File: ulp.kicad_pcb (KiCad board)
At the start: 2 copper layers, 102 x 84.2 mm, 49 parts, among them J1 Conn_01x01_Pin, J2 Conn_01x01_Pin, SW1 SW_Push_45deg, SW10 SW_Push_45deg, SW11 SW_Push_45deg, SW12 SW_Push_45deg, SW13 SW_Push_45deg, SW14 SW_Push_45deg, SW15 SW_Push_45deg, SW16 SW_Push_45deg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

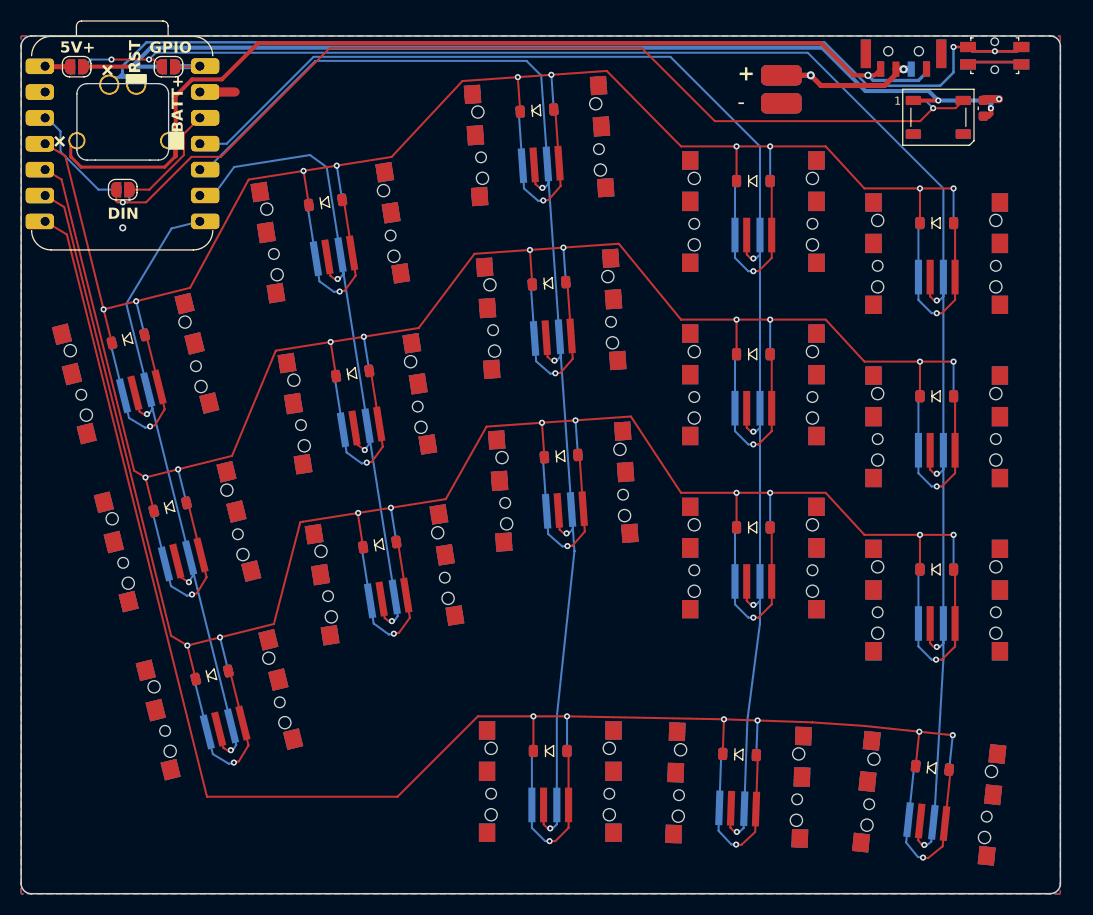
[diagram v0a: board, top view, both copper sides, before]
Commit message: change board outline
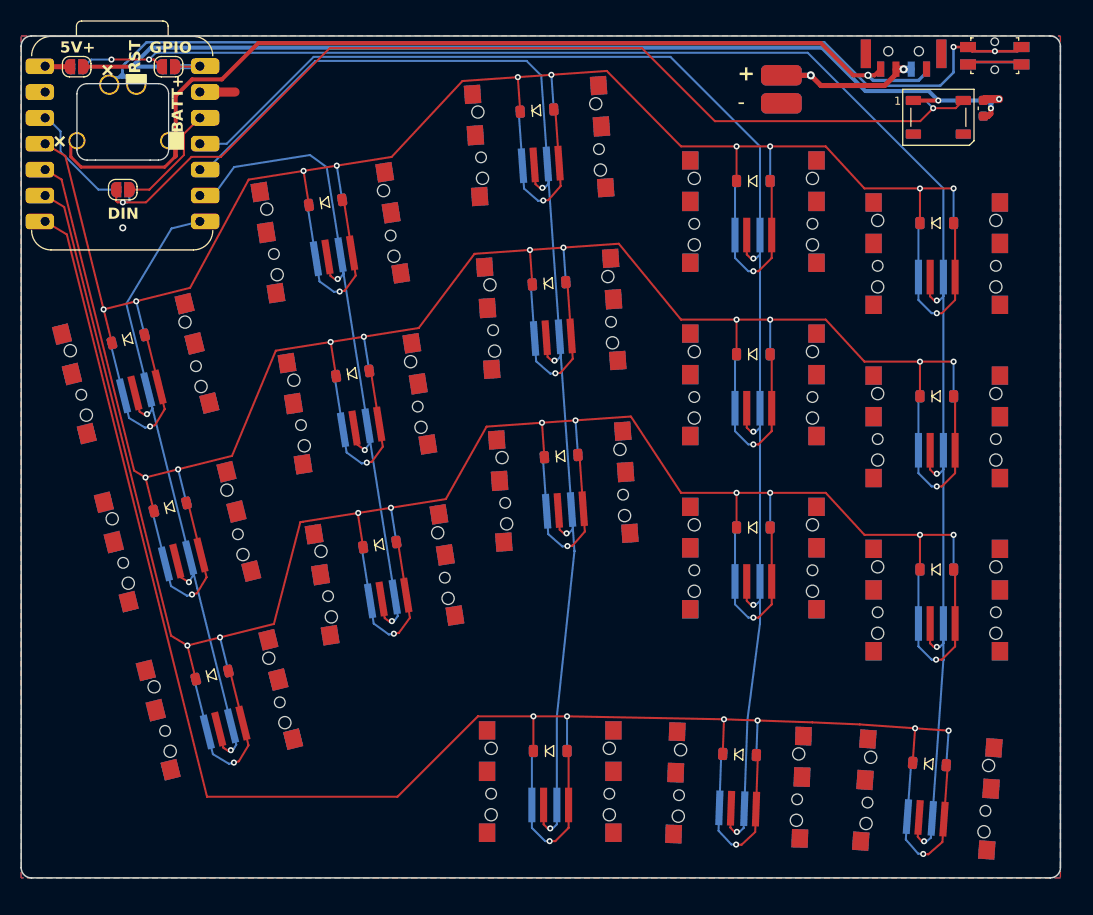
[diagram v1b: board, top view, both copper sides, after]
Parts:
- moved D18 0.48 mm to (187.8, 126.2), turned to -4 degrees
- moved SW18 0.42 mm to (187.6, 129.2), turned to -4 degrees
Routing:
- net /column 4: track 178.0 -> 179.0 mm
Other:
- board size 102 x 84.2 mm -> 102 x 82.6 mm

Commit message: test commit
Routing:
- net GND: track 15.9 -> 15.0 mm
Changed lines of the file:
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@@
+	)
+	(segment
+		(start 116.181622 60.267605)
+		(end 118.695537 60.267605)
+		(width 0.9)
+		(layer "F.Cu")
+		(net "GND")
 	)
 	(segment
@@
 		(layer "F.Cu")
 		(net "GND")
-	)
-	(segment
-		(start 116.181622 60.267605)
-		(end 119.642698 60.267606)
-		(width 0.9)
-		(layer "F.Cu")
-		(net "GND")

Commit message: add new pcb stuff
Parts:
- moved SW17 0.68 mm to (169.7, 128.2)
- moved D17 0.68 mm to (169.8, 125.2)
- moved SW16 0.68 mm to (151.2, 127.8)
- moved D16 0.68 mm to (151.2, 124.8)
- moved SW18 0.49 mm to (188.0, 129.0), turned to -3 degrees
- moved D18 0.45 mm to (188.2, 126.0), turned to -3 degrees
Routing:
- net GND: track 15.0 -> 15.9 mm
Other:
- board size 102 x 82.6 mm -> 102 x 82.2 mm

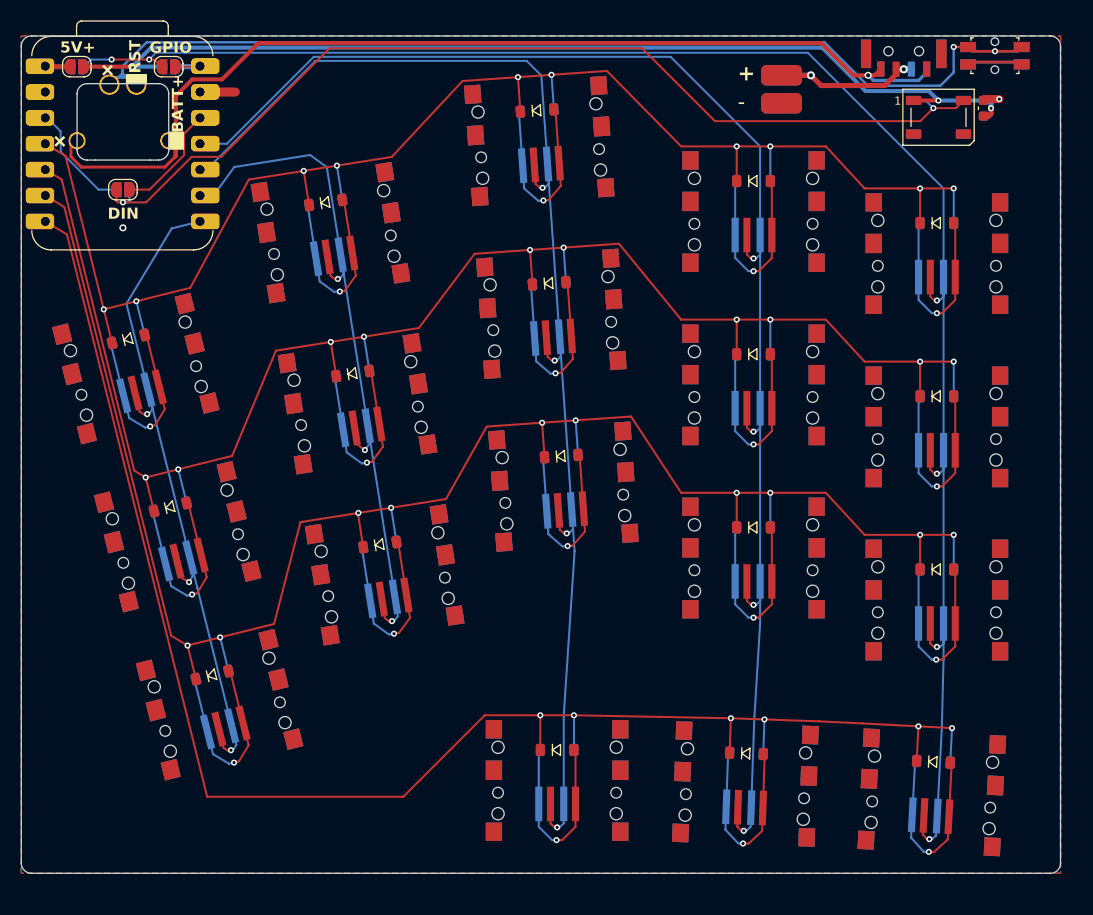
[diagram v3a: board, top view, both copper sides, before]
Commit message: add mounting holes and new models
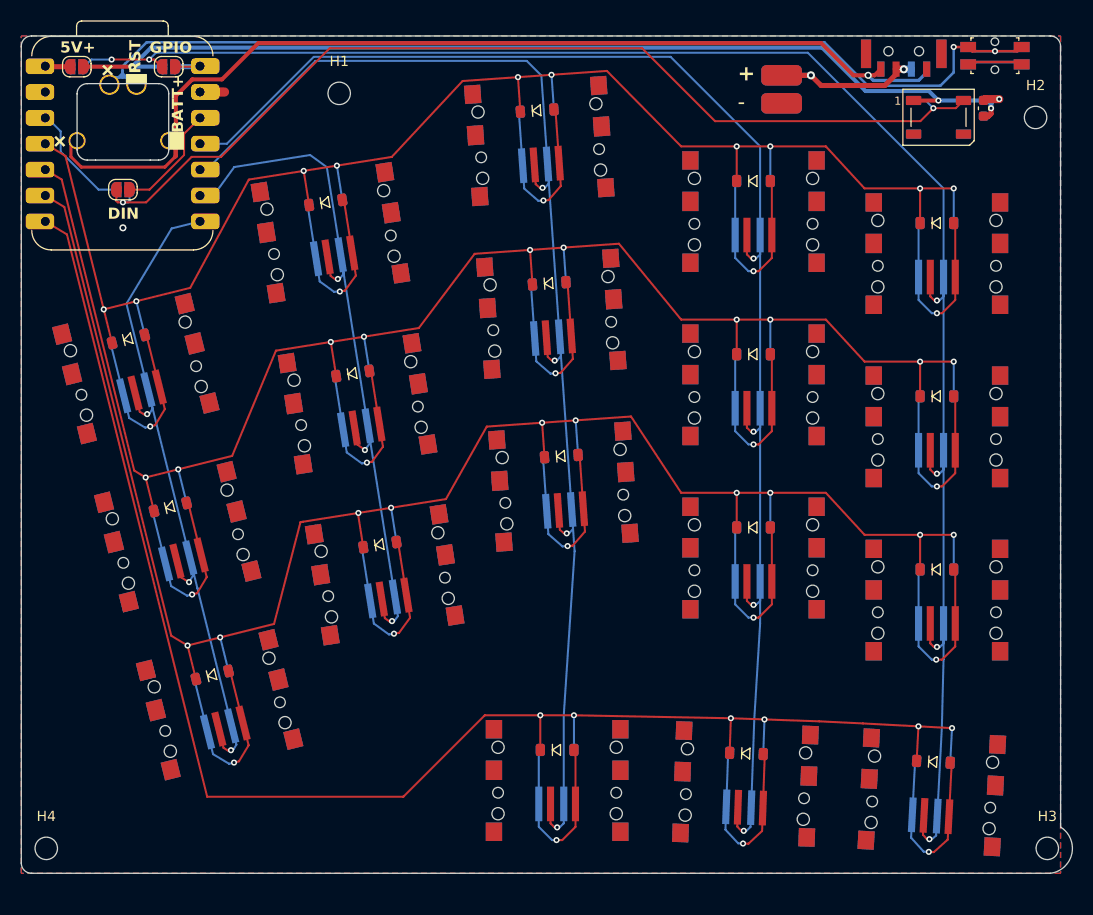
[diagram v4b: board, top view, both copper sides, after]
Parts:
- added H1: MountingHole, MountingHole:MountingHole_2.2mm_M2, F.Cu at (129.9, 60.4)
- added H2: MountingHole, MountingHole:MountingHole_2.2mm_M2, F.Cu at (198.2, 62.8)
- added H3: MountingHole, MountingHole:MountingHole_2.2mm_M2, F.Cu at (199.4, 134.5)
- added H4: MountingHole, MountingHole:MountingHole_2.2mm_M2, F.Cu at (101.1, 134.5)
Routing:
- net GND: track 15.9 -> 14.9 mm
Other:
- board size 102 x 82.2 mm -> 103.2 x 82.2 mm
